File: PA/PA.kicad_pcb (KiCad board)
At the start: 2 copper layers, 100 x 100 mm, 126 parts, among them J1 Conn_Coaxial, J10 Conn_01x01, J11 Conn_01x01, J12 Conn_01x01, J13 Conn_01x01, J14 Conn_01x01, J15 Conn_01x01, J16 Conn_01x01, J17 Conn_01x01, J18 Conn_01x01, J19 Conn_01x01, J2 Conn_01x02, J20 Conn_01x01, J21 Conn_01x01, J22 Conn_01x01, J23 Conn_01x01, J24 Conn_01x01, J25 Conn_01x01, J26 Conn_01x01, J27 Conn_01x01, J28 Conn_01x01, J3 Conn_Coaxial, J4 Conn_01x02, J5 Conn_01x02, J6 Conn_01x01, J7 Conn_01x01, J8 Conn_01x01, J9 Conn_01x01, Q1 2N3904, Q2 IRF510N, Q3 IRF510N, Q4 2N3906, Q5 IRF510N, Q6 2N3904, T1 Transformer_1P1Sdotted, T2 Transformer_1P1Sdotted, T3 Transformer_1P1Sdotted

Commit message: Some more comitization
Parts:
- added J29: Conn_01x01, Connectors:1pin, F.Cu at (82.1, 92.0)
- added J30: Conn_01x01, Connectors:1pin, F.Cu at (97.4, 106.0)
- moved C11 5.85 mm to (93.5, 42.9), turned to 270 degrees
- moved C5 3.43 mm to (71.7, 57.7)
- moved C13 3.25 mm to (96.6, 47.8), turned to 90 degrees
- moved JP5 2.01 mm to (93.8, 94.5)
- moved JP6 1.77 mm to (90.0, 94.5)
- moved R4 1.11 mm to (70.0, 81.7)
- moved R3 1.10 mm to (82.7, 85.9)
- moved T2 1.07 mm to (95.4, 57.5)
- moved C19 0.91 mm to (106.8, 56.4)
- moved T3 0.81 mm to (99.9, 68.4)
- moved D10 0.72 mm to (76.3, 54.9)
- moved J25 0.34 mm to (66.8, 87.7)
- moved L3 0.17 mm to (103.4, 42.1)
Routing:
- net Net-(C11-Pad1): track 63.5 -> 60.5 mm
- net Net-(JP5-Pad2): track 19.5 -> 22.2 mm
- net Net-(C5-Pad2): track 9.74 -> 7.54 mm
- net Net-(C1-Pad1): track 82.6 -> 80.5 mm
- net Net-(JP6-Pad2): track 23.8 -> 25.8 mm
- net Net-(C11-Pad2): track 2.16 -> 3.98 mm
- net FILTERIN: track 6.03 -> 7.78 mm
- net Net-(C12-Pad1): track 52.5 -> 53.9 mm
- net PASUPPLY: track 139.3 -> 140.1 mm
- net Net-(JP1-Pad2): track 7.55 -> 6.95 mm
- net Net-(JP1-Pad1): track 17.5 -> 17.0 mm
- removed copper zone on B.Cu, net GND

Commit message: Moved T!
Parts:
- moved D10 14.0 mm to (84.4, 66.3), turned to 270 degrees
- moved D8 3.58 mm to (84.4, 55.7), turned to 270 degrees
- moved C9 3.18 mm to (68.7, 57.5)
- moved T1 2.37 mm to (77.1, 67.6)
- moved RV1 2.11 mm to (67.2, 61.8)
- moved C7 1.98 mm to (63.1, 60.5)
- moved JP2 1.84 mm to (64.1, 53.9)
- moved R5 1.72 mm to (61.2, 70.4)
- moved JP1 1.44 mm to (67.9, 77.8)
- moved R6 0.98 mm to (74.0, 52.9)
- moved L1 0.91 mm to (64.1, 74.2)
- moved R9 0.73 mm to (67.2, 42.7)
- moved L2 0.67 mm to (70.5, 42.7)
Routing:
- net Net-(D10-Pad1): track 7.36 -> 3.05 mm
- net Net-(C1-Pad1): track 80.5 -> 84.4 mm
- net Net-(C9-Pad1): track 16.4 -> 13.4 mm
- net Net-(C11-Pad1): track 60.5 -> 58.1 mm
- net Net-(C5-Pad2): track 7.54 -> 5.87 mm
- net Net-(C6-Pad1): track 17.3 -> 15.9 mm
- net Net-(L2-Pad1): track 16.6 -> 15.2 mm
- net AMPINPUT: track 25.0 -> 23.6 mm
- net Net-(JP1-Pad2): track 6.95 -> 8.18 mm
- net +5V: track 218.6 -> 217.5 mm
- net Net-(JP1-Pad1): track 17.0 -> 16.4 mm

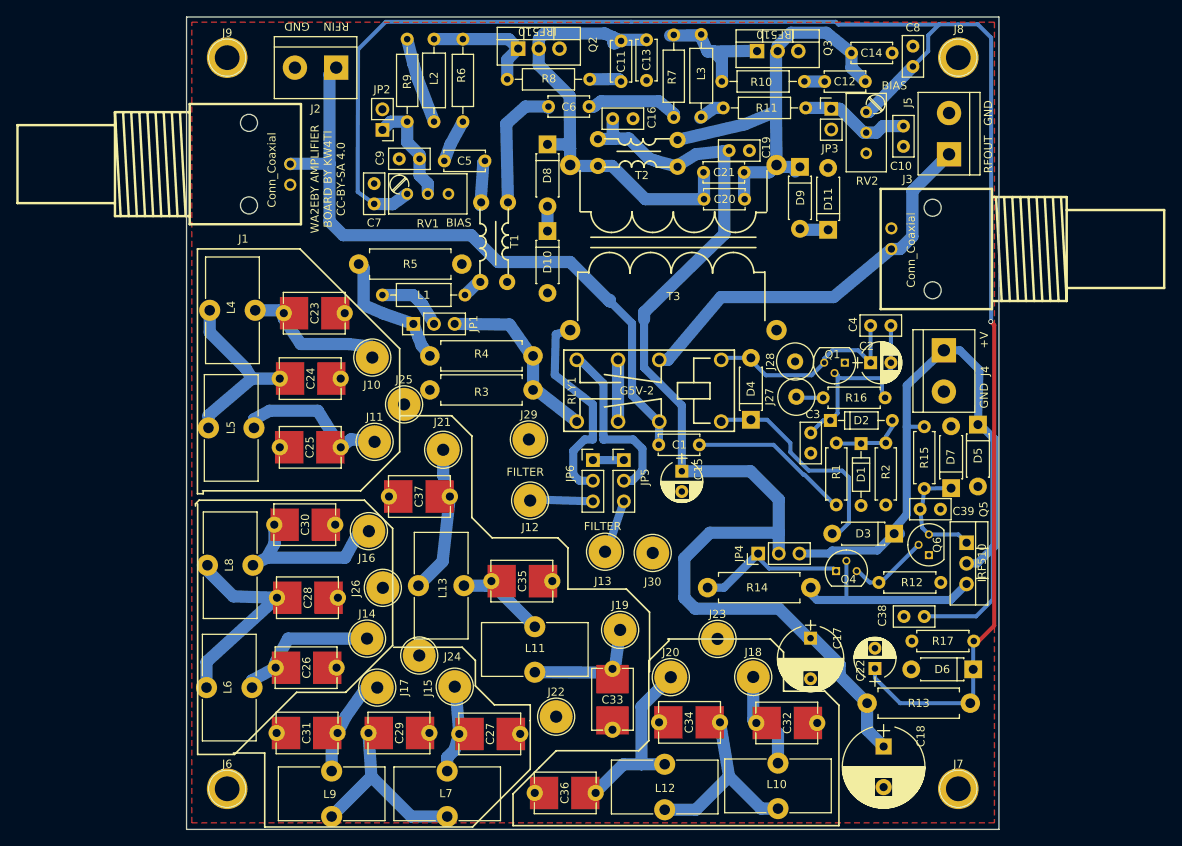
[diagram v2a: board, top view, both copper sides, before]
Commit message: Changed overcurrent circuit...
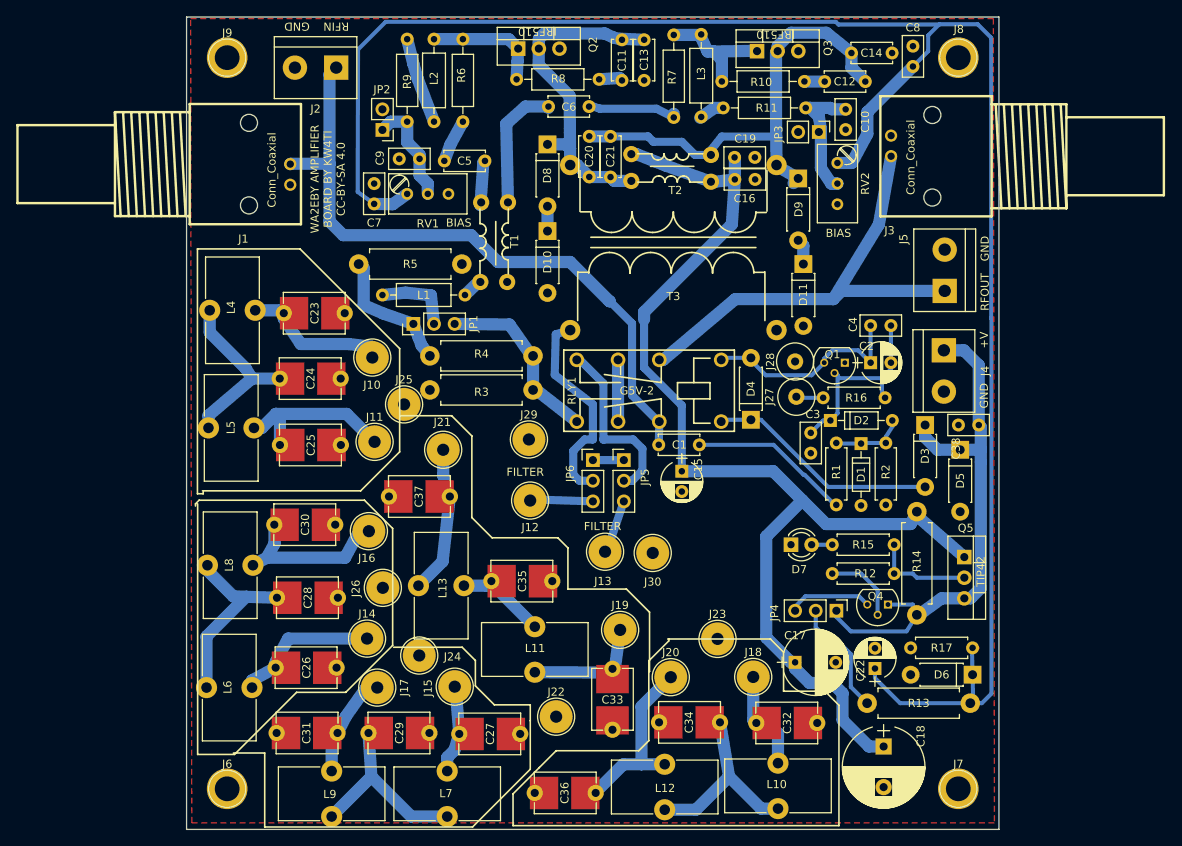
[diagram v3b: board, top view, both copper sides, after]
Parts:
- removed C39: 1 nF, Capacitors_THT:C_Disc_D5.0mm_W2.5mm_P2.50mm
- removed Q6: 2N3904, TO_SOT_Packages_THT:TO-92_Molded_Narrow
- D7: value 1N4744A -> LED; footprint Diodes_THT:D_DO-41_SOD81_P7.62mm_Horizontal -> LEDs:LED_D3.0mm
- Q5: value IRF510N -> TIP42
- moved R14 27.4 mm to (129.9, 100.9), turned to 270 degrees
- moved C38 24.5 mm to (137.5, 90.2)
- moved D7 20.9 mm to (114.4, 105.0), turned to 0 degrees
- moved J5 16.8 mm to (133.3, 73.7)
- moved C16 16.8 mm to (107.5, 60.0)
- moved R15 15.0 mm to (127.1, 105.0), turned to 180 degrees
- moved C20 14.4 mm to (89.6, 59.7), turned to 90 degrees
- moved D3 13.9 mm to (130.9, 90.2), turned to 270 degrees
- moved JP4 11.9 mm to (120.0, 113.1), turned to 270 degrees
- moved C21 11.5 mm to (92.2, 59.7), turned to 90 degrees
- moved J3 11.4 mm to (139.1, 57.1)
- moved Q4 7.60 mm to (126.3, 112.3), turned to 180 degrees
- moved C25 7.49 mm to (51.5, 92.7), turned to 0 degrees
- moved C10 7.41 mm to (121.1, 51.4)
- moved RV2 7.21 mm to (120.1, 58.0)
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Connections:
- D7 pad 1: Net-(C39-Pad1) -> GND
- D7 pad 2: GND -> Net-(D7-Pad2)
- JP4 pad 1: Net-(JP4-Pad1) -> +28V
- JP4 pad 2: PASUPPLY -> BIASSUPPLY
- JP4 pad 3: +28V -> Net-(JP4-Pad3)
- Q4 pad 1: Net-(JP4-Pad1) -> +28V
- Q4 pad 3: Net-(Q4-Pad3) -> Net-(JP4-Pad3)
- Q5 pad 1: Net-(C39-Pad1) -> PASUPPLY
- Q5 pad 2: +28V -> Net-(Q5-Pad2)
- Q5 pad 3: Net-(Q4-Pad2) -> +28V
- R12 pad 1: GND -> Net-(Q5-Pad2)
- R12 pad 2: Net-(Q4-Pad3) -> Net-(Q4-Pad2)
- R13 pad 2: PASUPPLY -> BIASSUPPLY
- R14 pad 1: Net-(JP4-Pad1) -> PASUPPLY
- R14 pad 2: Net-(Q4-Pad2) -> +28V
- R15 pad 1: +28V -> Net-(Q5-Pad2)
- R15 pad 2: Net-(C39-Pad1) -> Net-(D7-Pad2)
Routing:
- net +28V: track 89.0 -> 67.6 mm
- net Net-(JP4-Pad1): track 18.7 -> 0.00 mm
- net Net-(Q4-Pad2): track 26.4 -> 9.48 mm
- net +5V: track 217.5 -> 233.6 mm, vias 1 -> 0
- net Net-(C39-Pad1): track 15.1 -> 0.00 mm
- net Net-(C11-Pad1): track 58.1 -> 43.2 mm
- net BIASSUPPLY: track 0.00 -> 14.6 mm
- net Net-(Q5-Pad2): track 0.00 -> 12.4 mm
- net Net-(JP4-Pad3): track 0.00 -> 10.3 mm
- net Net-(Q4-Pad3): track 10.1 -> 0.00 mm
- net Net-(J3-Pad1): track 49.5 -> 57.6 mm
- net Net-(C12-Pad1): track 53.9 -> 59.1 mm
- net Net-(C10-Pad1): track 13.6 -> 16.8 mm
- net Net-(D7-Pad2): track 0.00 -> 2.54 mm
- net Net-(C25-Pad1): track 19.0 -> 21.0 mm
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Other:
- board text added: "TIP42"

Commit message: Added via fences
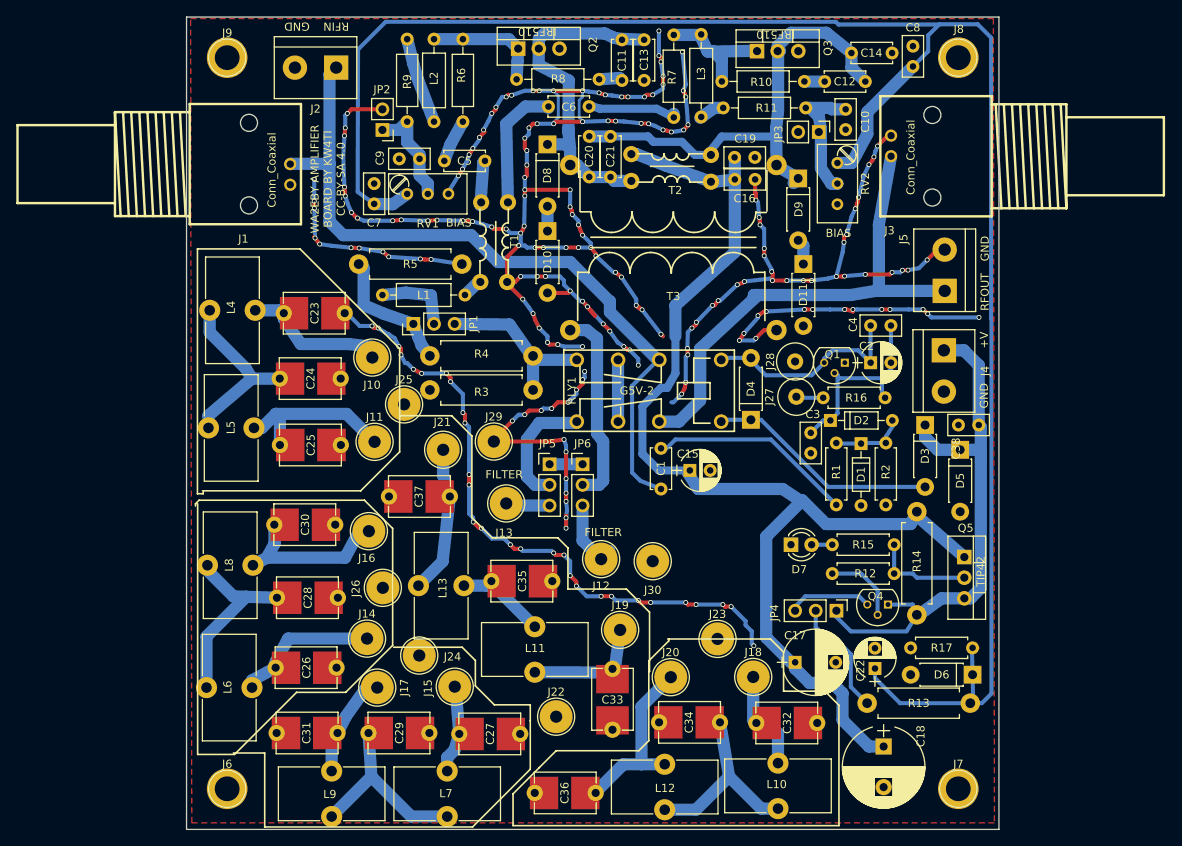
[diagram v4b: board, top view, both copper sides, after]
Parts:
- moved J13 13.5 mm to (79.3, 99.9)
- moved J12 11.3 mm to (91.0, 106.7)
- moved JP5 9.16 mm to (84.7, 95.0)
- moved C1 5.44 mm to (98.4, 98.1), turned to 90 degrees
- moved J29 4.33 mm to (77.8, 92.3)
- moved JP6 1.37 mm to (88.7, 95.0)
- moved J30 1.02 mm to (97.4, 107.0)
- moved C15 1.00 mm to (102.0, 95.8), turned to 0 degrees
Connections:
- RLY1 pad 2: Net-(C1-Pad1) -> Net-(J3-Pad1)
- RLY1 pad 4: AMPINPUT -> Net-(JP5-Pad2)
- RLY1 pad 6: Net-(J3-Pad1) -> Net-(C1-Pad1)
- RLY1 pad 8: Net-(JP5-Pad2) -> AMPINPUT
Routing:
- net GND: track 0.00 -> 474.4 mm, vias 0 -> 200
- net Net-(C1-Pad1): track 84.1 -> 93.9 mm
- net Net-(JP5-Pad2): track 22.2 -> 14.9 mm
- net Net-(J3-Pad1): track 57.6 -> 63.9 mm
- net Net-(C1-Pad2): track 19.9 -> 25.6 mm
- net PASUPPLY: track 140.9 -> 143.9 mm
- net Net-(JP6-Pad2): track 25.8 -> 24.2 mm
- net FILTEROUT: track 6.66 -> 5.44 mm
- net FILTERIN: track 7.78 -> 8.99 mm
- net Net-(C11-Pad1): track 43.2 -> 43.8 mm

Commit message: Added more convenient pads for TO220 devices
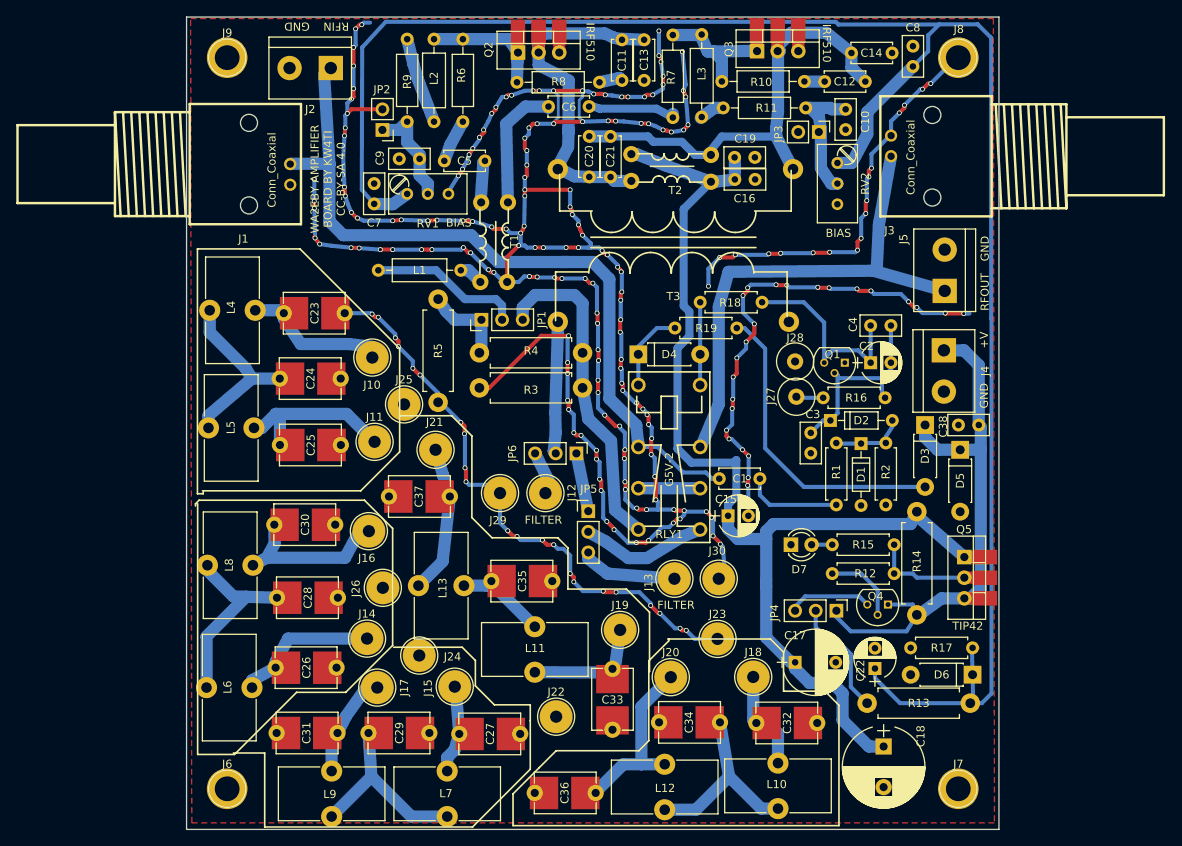
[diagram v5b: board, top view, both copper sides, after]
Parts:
- removed D10, D11, D8, D9: ZENER, Diodes_THT:D_DO-41_SOD81_P7.62mm_Horizontal
- added R18: 0R, Resistors_THT:R_Axial_DIN0207_L6.3mm_D2.5mm_P7.62mm_Horizontal, F.Cu at (110.8, 75.1)
- added R19: 0R, Resistors_THT:R_Axial_DIN0207_L6.3mm_D2.5mm_P7.62mm_Horizontal, F.Cu at (107.7, 78.3)
- Q2, Q3, Q5: footprint TO_SOT_Packages_THT:TO-220-3_Vertical -> PA:TO-220-3_Vertical_WithPads
- moved J13 22.7 mm to (100.1, 109.1)
- moved D4 16.0 mm to (95.6, 81.5), turned to 0 degrees
- moved R5 10.7 mm to (71.0, 74.7), turned to 270 degrees
- moved J12 10.6 mm to (84.2, 98.6)
- moved J30 8.41 mm to (105.5, 109.1)
- moved JP1 8.40 mm to (76.3, 77.3)
- moved JP5 7.49 mm to (89.4, 100.8)
- moved C15 7.30 mm to (106.7, 101.4)
- moved C1 7.29 mm to (105.6, 96.8), turned to 0 degrees
- moved J29 6.40 mm to (78.6, 98.6)
- moved R4 6.11 mm to (76.0, 81.3)
- moved R3 6.10 mm to (88.7, 85.6)
- moved RLY1 4.36 mm to (99.4, 87.7), turned to 270 degrees
- moved L1 3.09 mm to (63.6, 71.2)
- moved JP6 1.54 mm to (88.0, 93.7), turned to 270 degrees
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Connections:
- D4 pad 1: Net-(D3-Pad2) -> Net-(D4-Pad1)
- D4 pad 2: Net-(C2-Pad1) -> Net-(D4-Pad2)
- RLY1 pad 1: Net-(D3-Pad2) -> Net-(D4-Pad2)
- RLY1 pad 5: Net-(C2-Pad1) -> Net-(D4-Pad1)
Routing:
- net GND: track 474.4 -> 547.6 mm, vias 200 -> 220
- net AMPINPUT: track 23.3 -> 40.4 mm
- net Net-(C1-Pad2): track 25.6 -> 12.1 mm
- net Net-(D4-Pad2): track 0.00 -> 10.4 mm
- net Net-(D4-Pad1): track 0.00 -> 10.4 mm
- net Net-(D3-Pad2): track 28.9 -> 38.5 mm
- net Net-(JP1-Pad2): track 9.54 -> 18.8 mm
- net Net-(JP6-Pad2): track 24.2 -> 16.3 mm
- net FILTEROUT: track 5.44 -> 12.0 mm
- net Net-(JP1-Pad1): track 16.4 -> 10.7 mm
- net Net-(C1-Pad1): track 93.9 -> 97.7 mm
- net Net-(D11-Pad1): track 3.42 -> 0.00 mm
- net FILTERIN: track 8.99 -> 5.68 mm
- net AMPOUTPUT: track 4.06 -> 7.26 mm
- net PASUPPLY: track 143.9 -> 140.7 mm
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
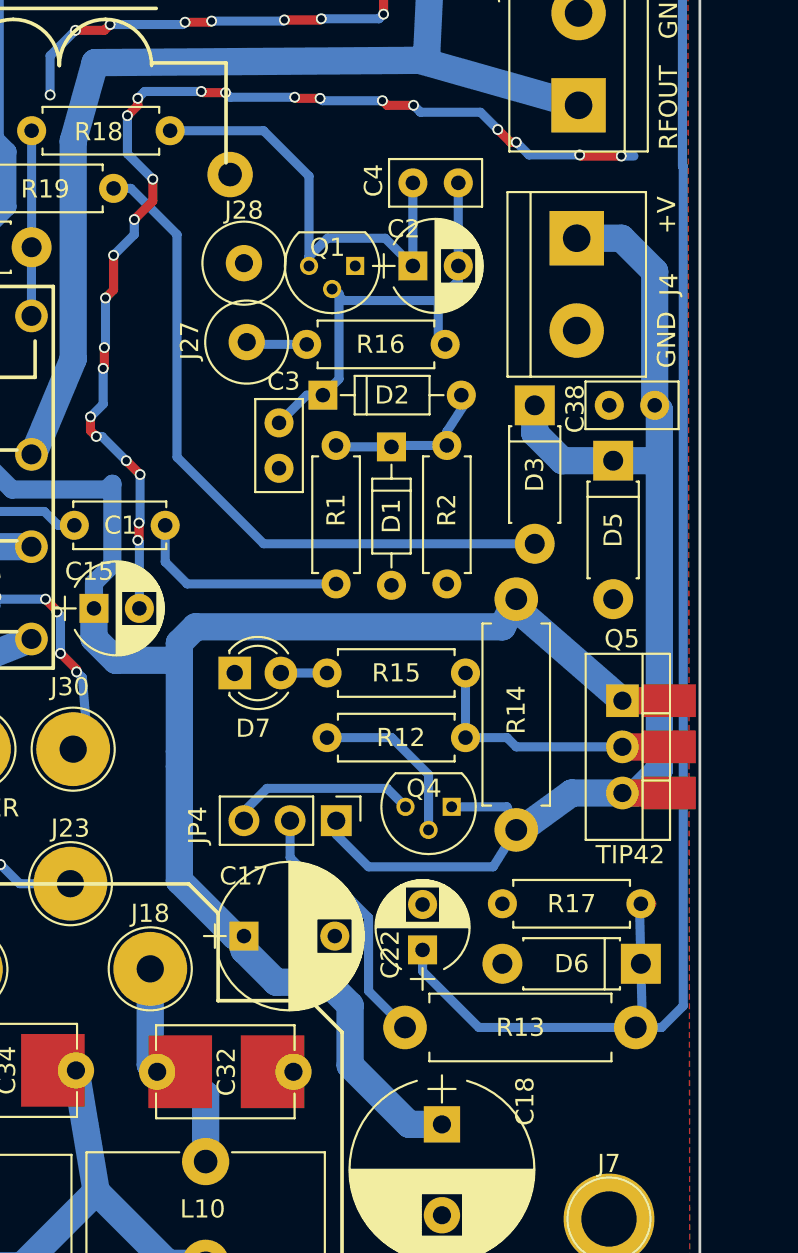
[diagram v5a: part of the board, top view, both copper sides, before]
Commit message: JLCPCB order tested
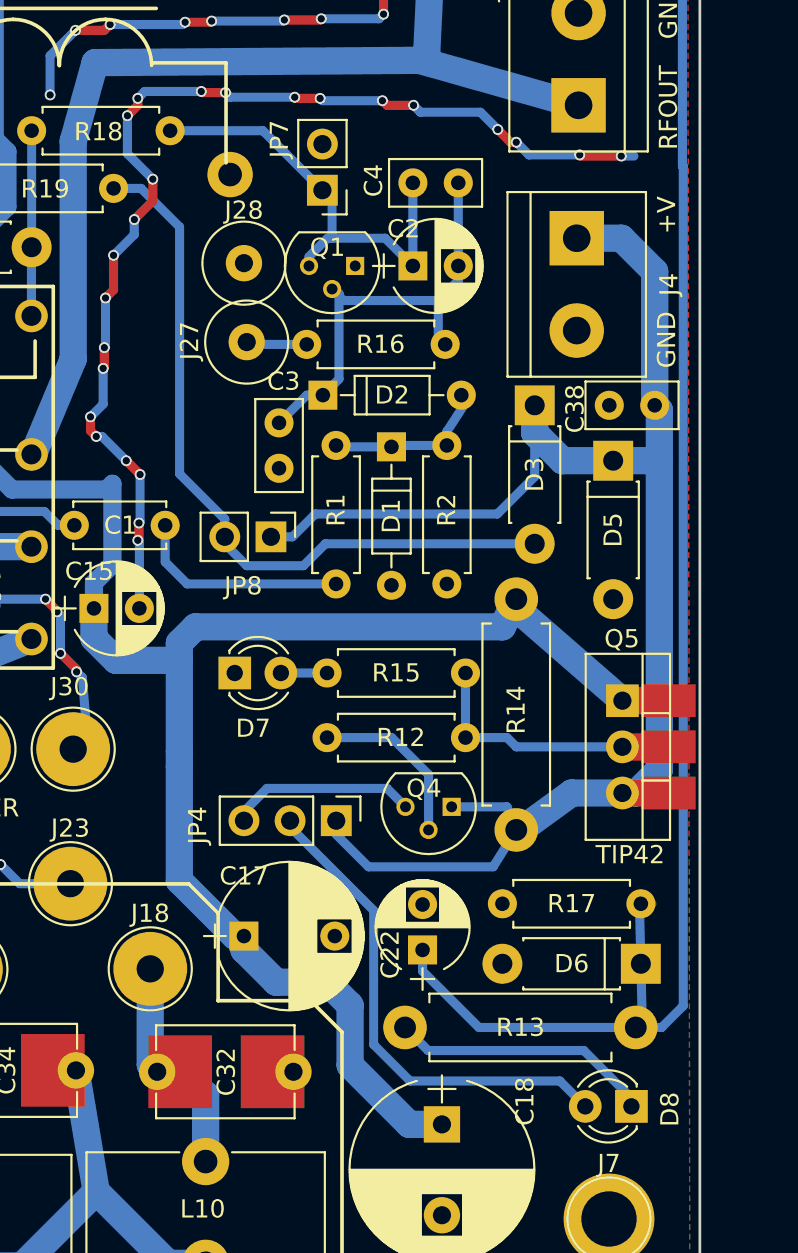
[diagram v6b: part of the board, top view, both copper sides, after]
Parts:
- added D8: LED, LEDs:LED_D3.0mm, F.Cu at (136.2, 128.8)
- added JP7: Jumper_NC_Small, Pin_Headers:Pin_Header_Straight_1x02_Pitch2.54mm, F.Cu at (119.2, 78.4)
- added JP8: Jumper_NC_Small, Pin_Headers:Pin_Header_Straight_1x02_Pitch2.54mm, F.Cu at (116.4, 97.5)
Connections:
- R13 pad 2: BIASSUPPLY -> Net-(D8-Pad1)
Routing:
- net +28V: track 70.1 -> 90.0 mm
- net Net-(D8-Pad1): track 0.00 -> 14.5 mm
- net BIASSUPPLY: track 14.6 -> 27.3 mm
- net Net-(D3-Pad2): track 38.5 -> 41.0 mm
- net Net-(C2-Pad1): track 25.5 -> 24.4 mm
